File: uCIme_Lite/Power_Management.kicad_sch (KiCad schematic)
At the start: 12 parts

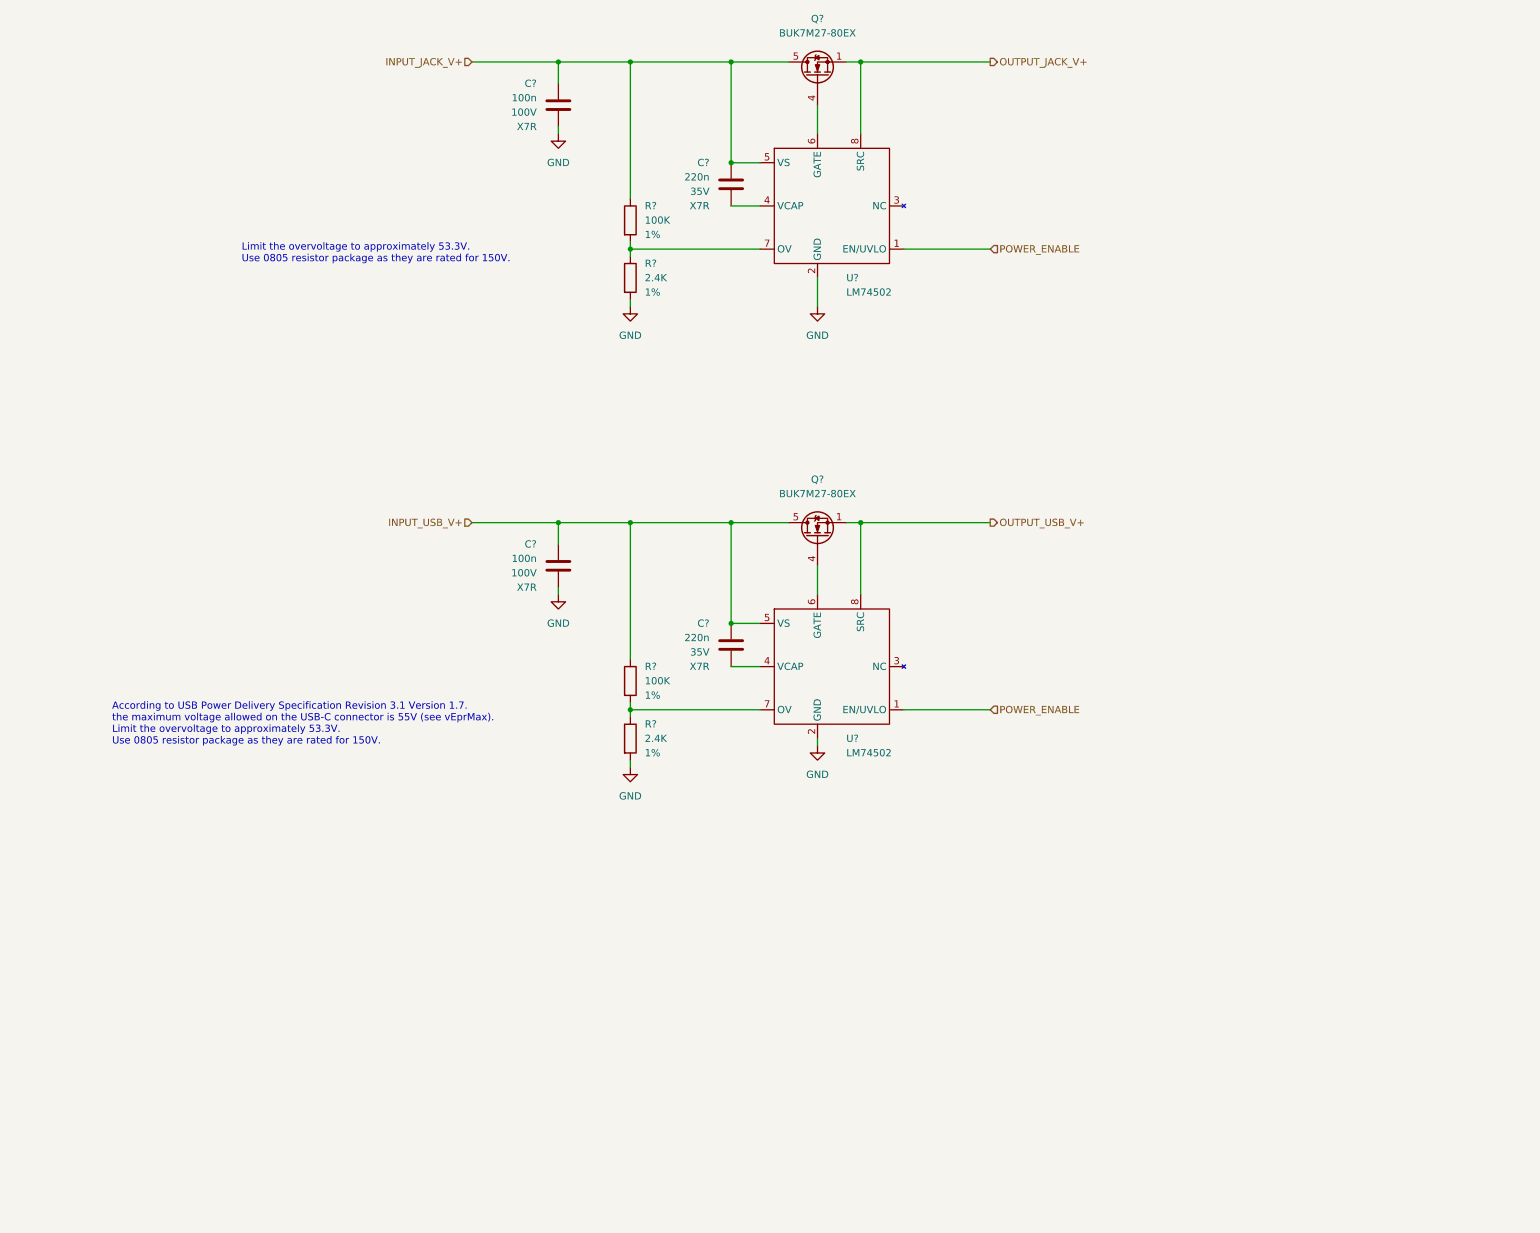
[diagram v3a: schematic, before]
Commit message: lite: Added jumpers to control the power channel mode (always enabled, always disabled or controlled by a FTDI GPIO).
Signed-off-by: Adrien Ricciardi <aricciardi@baylibre.com>
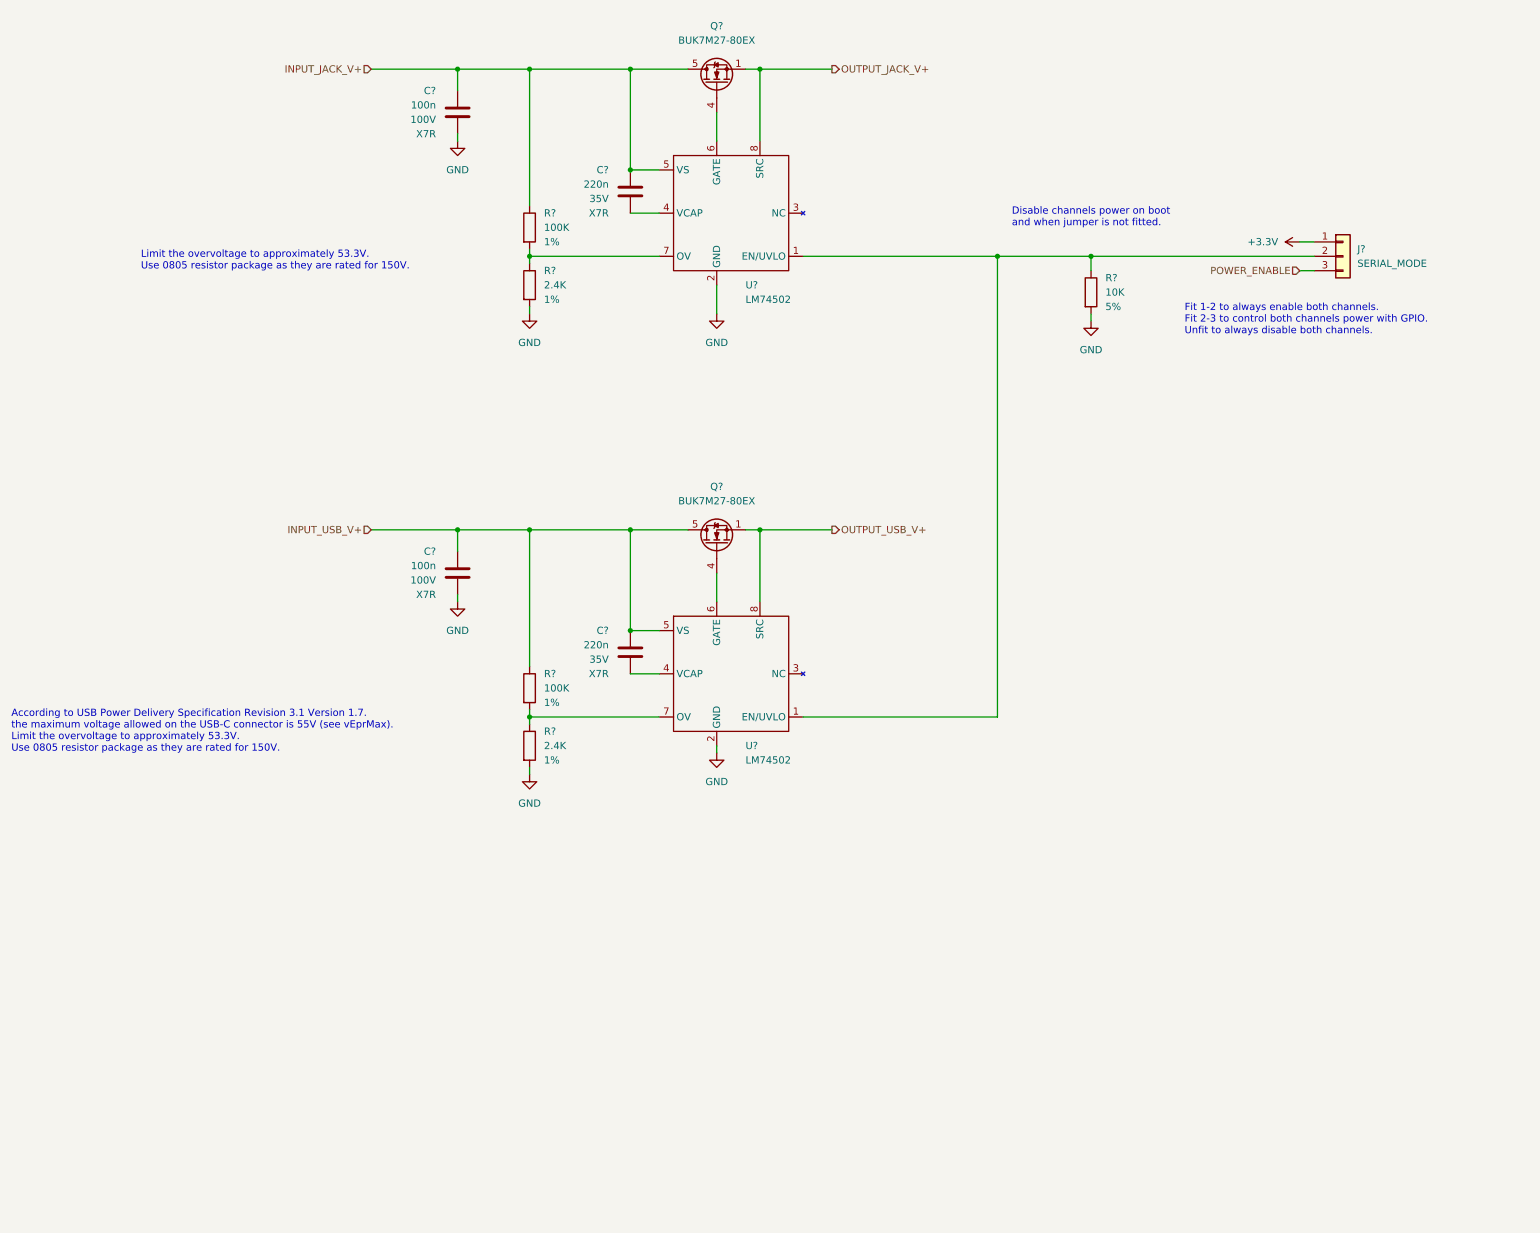
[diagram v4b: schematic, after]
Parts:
- added J?: SERIAL_MODE, symbol Connector_Generic:Conn_01x03
- added R?: 10K, Resistor_SMD:R_0603_1608Metric, symbol Device:R
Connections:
- net GND: now also R?.2
- net POWER_ENABLE: now also J?.3 (Pin_3); no longer U?.1 (EN/UVLO), U?.1 (EN/UVLO)
- new net: J?.2 (Pin_2), R?.1, U?.1 (EN/UVLO), U?.1 (EN/UVLO)
- new net +3.3V: J?.1 (Pin_1)
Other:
- note added: "Disable channels power on boot and when jumper is not fitted."
- note added: "Fit 1-2 to always enable both channels. Fit 2-3 to control both channels power with GPIO. Unfit to always disable both channels."
- moved on the sheet: C?, Q?, R?, U?

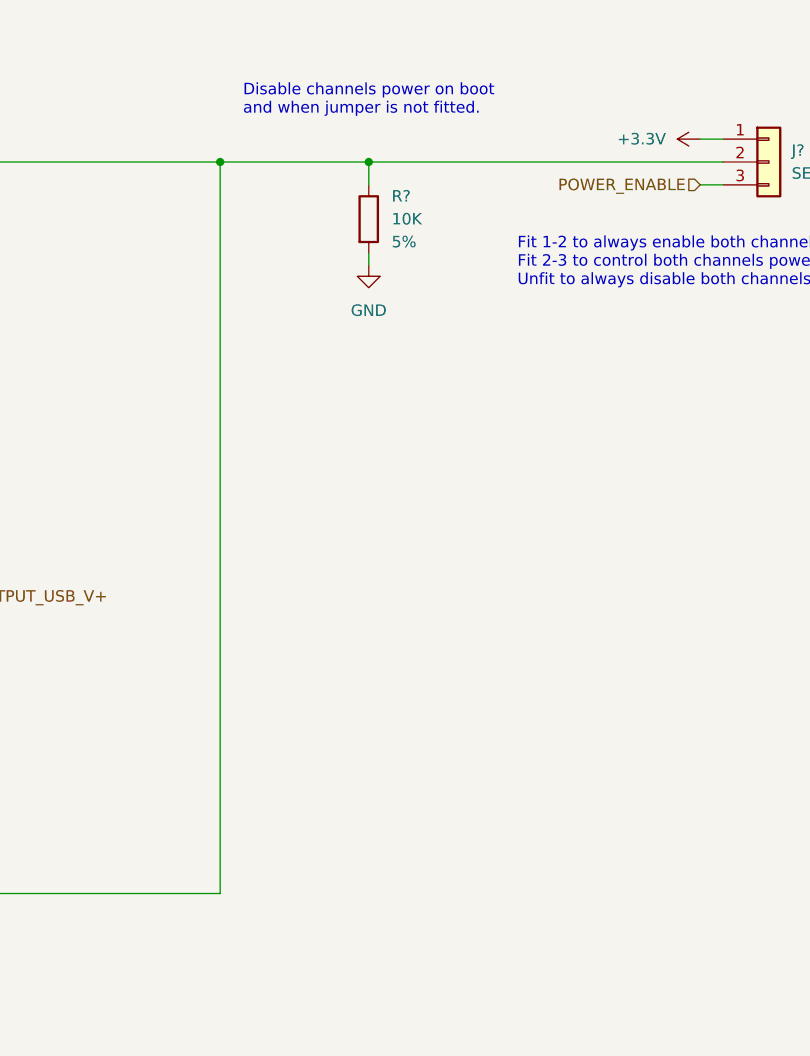
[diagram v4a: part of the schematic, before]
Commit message: lite: Added leds to schematic. One led for power switch, and two for UART TX and RX.
Signed-off-by: Adrien Ricciardi <aricciardi@baylibre.com>
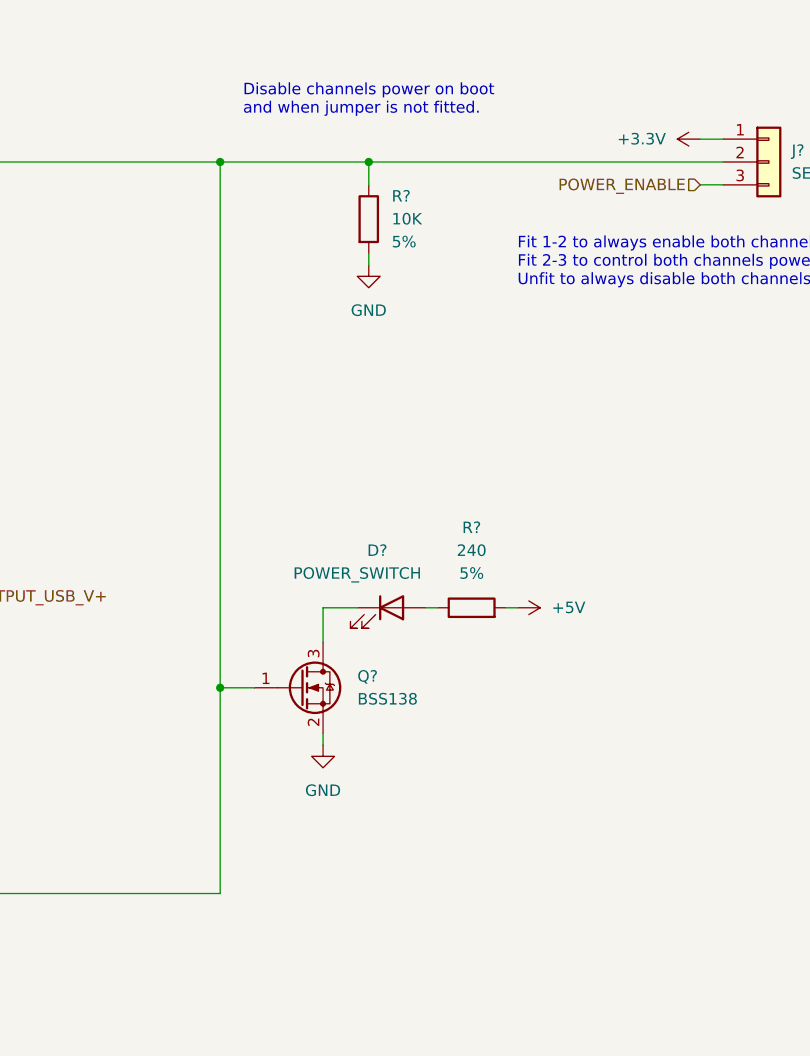
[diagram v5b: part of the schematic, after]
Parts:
- added D?: POWER_SWITCH, symbol Device:LED
- added Q?: BSS138, Package_TO_SOT_SMD:SOT-23, symbol Transistor_FET:BSS138
- added R?: 240, Resistor_SMD:R_1206_3216Metric, symbol Device:R
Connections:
- net GND: now also Q?.2 (S)
- net at J?.2 (Pin_2), R?.1, U?.1 (EN/UVLO)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: now also Q?.1 (G)
- new net: D?.1 (K), Q?.3 (D)
- new net: D?.2 (A), R?.1
- new net +5V: R?.2
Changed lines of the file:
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@@
   (junction (at 114.3 27.94) (diameter 0) (color 0 0 0 0)
   )
+  (junction (at 196.85 119.38) (diameter 0) (color 0 0 0 0)
+  )
   (junction (at 101.6 109.22) (diameter 0) (color 0 0 0 0)
   )
@@
     (stroke (width 0) (type default) (color 0 0 0 0))
   )
+  (wire (pts (xy 208.28 124.46) (xy 208.28 125.73))
+    (stroke (width 0) (type default) (color 0 0 0 0))
+  )
   (wire (pts (xy 152.4 27.94) (xy 154.94 27.94))
     (stroke (width 0) (type default) (color 0 0 0 0))
@@
     (stroke (width 0) (type default) (color 0 0 0 0))
   )
+  (wire (pts (xy 208.28 114.3) (xy 208.28 110.49))
+    (stroke (width 0) (type default) (color 0 0 0 0))
+  )
   (wire (pts (xy 162.56 60.96) (xy 196.85 60.96))
     (stroke (width 0) (type default) (color 0 0 0 0))
@@
     (stroke (width 0) (type default) (color 0 0 0 0))
   )
+  (wire (pts (xy 208.28 110.49) (xy 212.09 110.49))
+    (stroke (width 0) (type default) (color 0 0 0 0))
+  )
   (wire (pts (xy 114.3 60.96) (xy 114.3 62.23))
     (stroke (width 0) (type default) (color 0 0 0 0))
@@
     (stroke (width 0) (type default) (color 0 0 0 0))
   )
+  (wire (pts (xy 228.6 110.49) (xy 229.87 110.49))
+    (stroke (width 0) (type default) (color 0 0 0 0))
+  )
   (wire (pts (xy 154.94 109.22) (xy 154.94 121.92))
     (stroke (width 0) (type default) (color 0 0 0 0))
   )
-  (wire (pts (xy 196.85 142.24) (xy 196.85 60.96))
+  (wire (pts (xy 196.85 142.24) (xy 196.85 119.38))
+    (stroke (width 0) (type default) (color 0 0 0 0))
+  )
+  (wire (pts (xy 196.85 119.38) (xy 196.85 60.96))
     (stroke (width 0) (type default) (color 0 0 0 0))
   )
@@
     (stroke (width 0) (type default) (color 0 0 0 0))
   )
+  (wire (pts (xy 196.85 119.38) (xy 200.66 119.38))
+    (stroke (width 0) (type default) (color 0 0 0 0))
+  )
   (wire (pts (xy 101.6 120.65) (xy 101.6 121.92))
     (stroke (width 0) (type default) (color 0 0 0 0))
@@
   )
   (wire (pts (xy 250.19 58.42) (xy 252.73 58.42))
+    (stroke (width 0) (type default) (color 0 0 0 0))
+  )
+  (wire (pts (xy 219.71 110.49) (xy 220.98 110.49))
     (stroke (width 0) (type default) (color 0 0 0 0))
   )
@@
     (pin "1")
     (pin "2")
+  )
+  (symbol (lib_id "power:GND") (at 208.28 125.73 0) (unit 1)
+    (in_bom yes) (on_board yes) (fields_autoplaced)
+    (property "Reference" "#PWR?" (id 0) (at 208.28 132.08 0)
+      (effects (font (size 1.27 1.27)) hide)
+    )
+    (property "Value" "GND" (id 1) (at 208.28 130.81 0))
+    (property "Footprint" "" (id 2) (at 208.28 125.73 0)
+      (effects (font (size 1.27 1.27)) hide)
+    )
+    (property "Datasheet" "" (id 3) (at 208.28 125.73 0)
+      (effects (font (size 1.27 1.27)) hide)
+    )
+    (pin "1")
   )
   (symbol (lib_id "Device:C") (at 101.6 35.56 0) (unit 1)
@@
     (pin "8")
   )
+  (symbol (lib_id "Device:LED") (at 215.9 110.49 0) (unit 1)
+    (in_bom yes) (on_board yes)
+    (property "Reference" "D?" (id 0) (at 214.3125 104.14 0))
+    (property "Value" "POWER_SWITCH" (id 1) (at 212.09 106.68 0))
+    (property "Footprint" "" (id 2) (at 215.9 110.49 0)
+      (effects (font (size 1.27 1.27)) hide)
+    )
+    (property "Datasheet" "" (id 3) (at 215.9 110.49 0)
+      (effects (font (size 1.27 1.27)) hide)
+    )
+    (property "Datasheet" "~" (id 4) (at 215.9 110.49 0)
+      (effects (font (size 1.27 1.27)) hide)
+    )
+    (property "Reference" "D?" (id 5) (at 215.9 110.49 0)
+      (effects (font (size 1.27 1.27)) hide)
+    )
+    (property "Value" "POWER_SWITCH" (id 6) (at 215.9 110.49 0)
+      (effects (font (size 1.27 1.27)) hide)
+    )
+    (pin "1")
+    (pin "2")
+  )
   (symbol (lib_id "power:GND") (at 101.6 40.64 0) (unit 1)
     (in_bom yes) (on_board yes) (fields_autoplaced)
@@
     (pin "1")
   )
+  (symbol (lib_id "power:+5V") (at 229.87 110.49 270) (unit 1)
+    (in_bom yes) (on_board yes) (fields_autoplaced)
+    (property "Reference" "#PWR?" (id 0) (at 226.06 110.49 0)
+      (effects (font (size 1.27 1.27)) hide)
+    )
+    (property "Value" "+5V" (id 1) (at 233.68 110.4899 90)
+      (effects (font (size 1.27 1.27)) (justify left))
+    )
+    (property "Footprint" "" (id 2) (at 229.87 110.49 0)
+      (effects (font (size 1.27 1.27)) hide)
+    )
+    (property "Datasheet" "" (id 3) (at 229.87 110.49 0)
+      (effects (font (size 1.27 1.27)) hide)
+    )
+    (pin "1")
+  )
   (symbol (lib_id "Device:C") (at 101.6 116.84 0) (unit 1)
     (in_bom yes) (on_board yes) (fields_autoplaced)
@@
     (pin "5")
   )
+  (symbol (lib_id "Transistor_FET:BSS138") (at 205.74 119.38 0) (unit 1)
+    (in_bom yes) (on_board yes) (fields_autoplaced)
+    (property "Reference" "Q?" (id 0) (at 212.09 118.1099 0)
+      (effects (font (size 1.27 1.27)) (justify left))
+    )
+    (property "Value" "BSS138" (id 1) (at 212.09 120.6499 0)
+      (effects (font (size 1.27 1.27)) (justify left))
+    )
+    (property "Footprint" "Package_TO_SOT_SMD:SOT-23" (id 2) (at 210.82 121.285 0)
+      (effects (font (size 1.27 1.27) italic) (justify left) hide)
+    )
+    (property "Datasheet" "https://www.onsemi.com/pub/Collateral/BSS138-D.PDF" (id 3) (at 205.74 119.38 0)
+      (effects (font (size 1.27 1.27)) (justify left) hide)
+    )
+    (property "PartNumber" "BSS138P,215" (id 4) (at 205.74 119.38 0)
+      (effects (font (size 1.27 1.27)) hide)
+    )
+    (pin "1")
+    (pin "2")
+    (pin "3")
+  )
+  (symbol (lib_id "Device:R") (at 224.79 110.49 90) (unit 1)
+    (in_bom yes) (on_board yes) (fields_autoplaced)
+    (property "Reference" "R?" (id 0) (at 224.79 101.6 90))
+    (property "Value" "240" (id 1) (at 224.79 104.14 90))
+    (property "Footprint" "Resistor_SMD:R_1206_3216Metric" (id 2) (at 224.79 112.268 90)
+      (effects (font (size 1.27 1.27)) hide)
+    )
+    (property "Datasheet" "~" (id 3) (at 224.79 110.49 0)
+      (effects (font (size 1.27 1.27)) hide)
+    )
+    (property "PartNumber" "" (id 4) (at 224.79 110.49 0)
+      (effects (font (size 1.27 1.27)) hide)
+    )
+    (property "Value1" "5%" (id 5) (at 224.79 106.68 90))
+    (pin "1")
+    (pin "2")
+  )
   (symbol (lib_id "Connector_Generic:Conn_01x03") (at 257.81 60.96 0) (unit 1)
